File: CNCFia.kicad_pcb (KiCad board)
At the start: 2 copper layers, 81.3 x 85.7 mm, 57 parts, among them J1 5V_OUT, J10 Driver_X, J11 Driver_Y, J12 Driver_Z, J13 Coolant, J14 Spin_10V, J15 Spin_Enabl, J16 Spin_Dir, J17 Mist, J2 IN_EXT_5V, J3 Limit SW_XY, J4 Limit SW_ZA, J5 Extra SW 0, J6 Extra SW 0, J7 IN_EXT_12V, J9 Signal Input, M1 MountingHole_3.2mm_M3, M2 MountingHole_3.2mm_M3, M3 MountingHole_3.2mm_M3, M4 MountingHole_3.2mm_M3, U1 LTV-847, U10 NTJD5121N, U11 NTJD5121N, U12 NTJD5121N, U2 LTV-847, U3 NTJD5121N, U4 NTJD5121N, U5 LM358P, U6 24LC16, U7 NTJD5121N, U8 NTJD5121N, U9 NTJD5121N

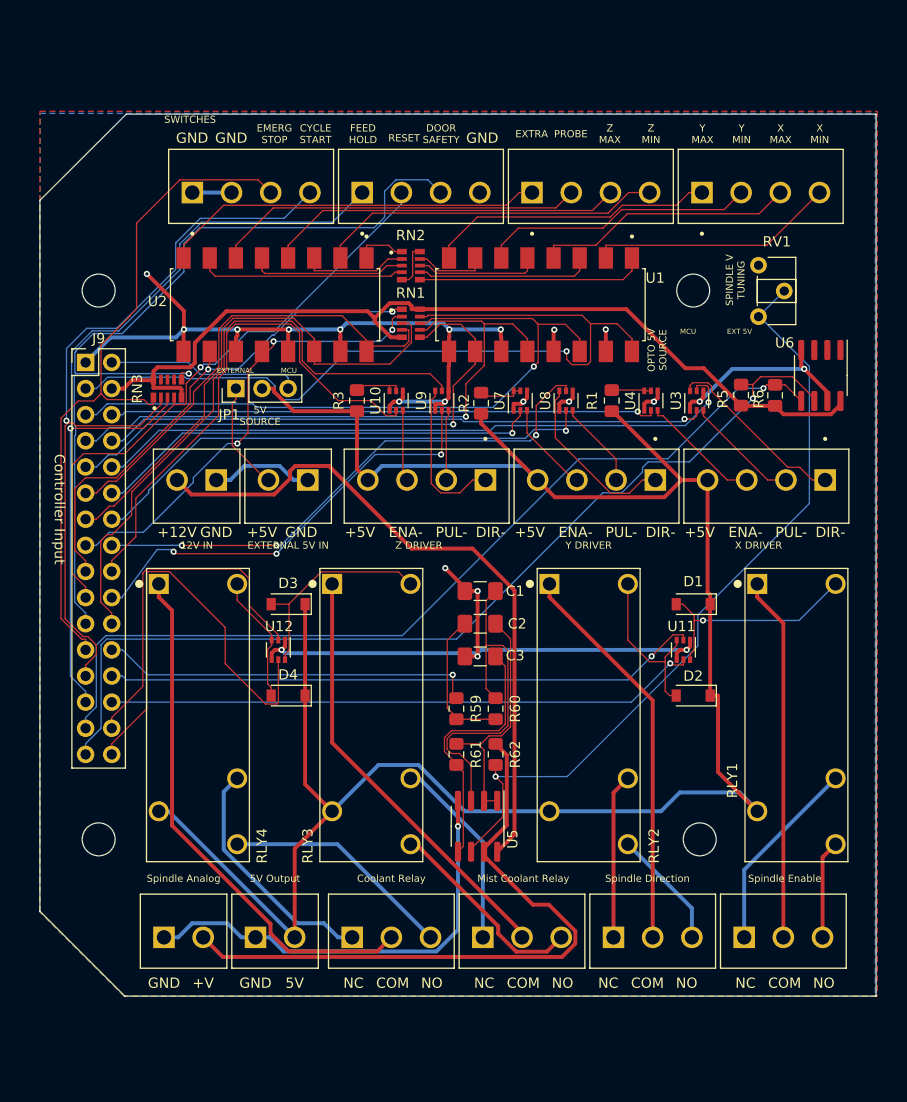
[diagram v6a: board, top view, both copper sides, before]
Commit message: Cosmetic and text changes
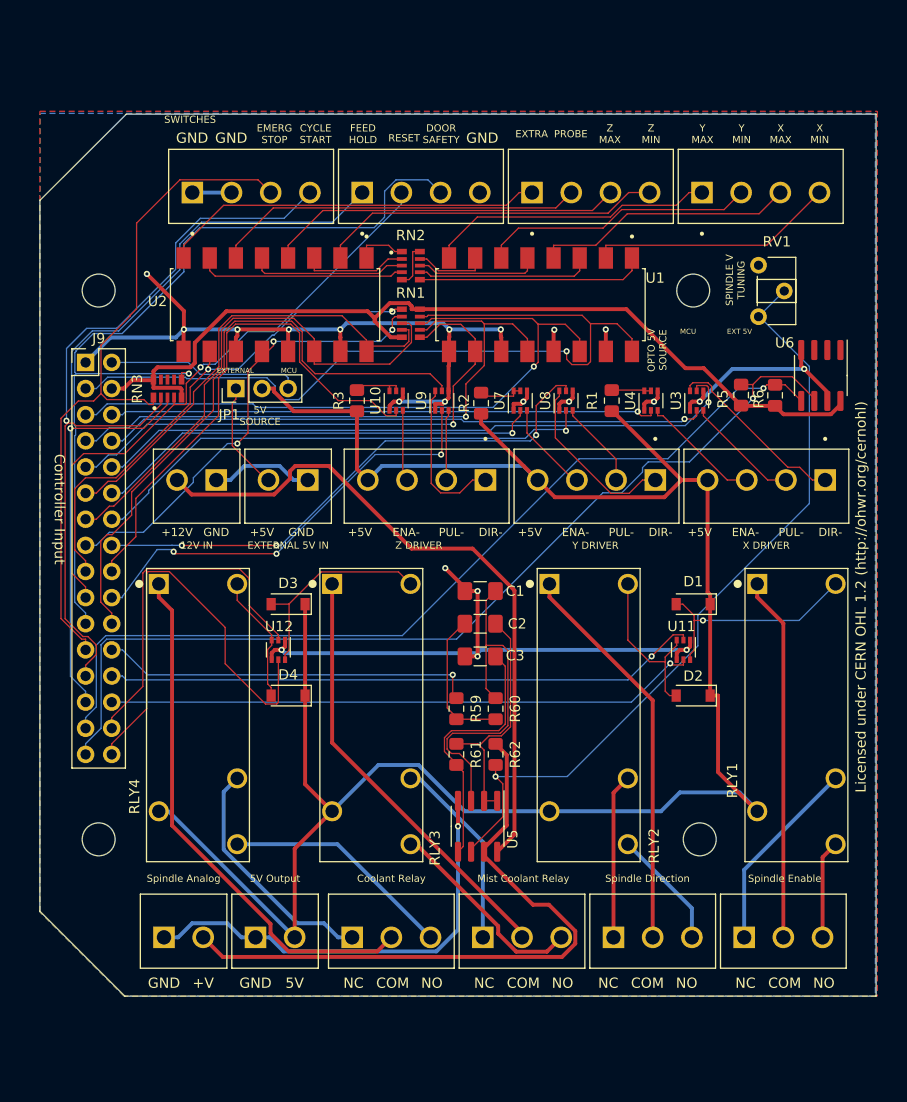
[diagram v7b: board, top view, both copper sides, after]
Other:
- board text added: "Licensed under CERN OHL 1.2 (http://ohwr.org/cernohl)"
